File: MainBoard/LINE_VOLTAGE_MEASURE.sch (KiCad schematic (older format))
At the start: 19 parts

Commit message: R0.1
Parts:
- removed D?: D, symbol Device:D
- removed D?: 6V, symbol Device:D_Zener
- removed R?: 1k, symbol Device:R
- removed R?: 1M, symbol Device:R
- removed R?: 25k, symbol Device:R
- removed U? (x5): LMV324, symbol Amplifier_Operational:LMV324
- added C?: 0.1uF, symbol Device:C
- added D?: 1N750, symbol Device:D_Zener
- added D?: D_Schottky, symbol Device:D_Schottky
- added R?: 1M, symbol Device:R
- added R?: 68, symbol Device:R
- added U? (x4): MCP6004, symbol Amplifier_Operational:MCP6004
- C?: value 33uF -> 10uF
- R?: value 1M -> 560k
- R?: value 15k -> 12k
- R?: value 4.7k -> 15k
- R?: footprint (none) -> Option in Mechatronics
- R?: value 4.7k -> 500k
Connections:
- net labels added: +6V
- net labels removed: +12V
- wire segments 62 -> 59
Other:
- note added: "A"
- note added: "A (Vrms)\n2.098\n2.308\n2.517\n2.727\n2.937\n"
- note added: "B"
- note added: "B (VDC)\n2.967\n3.264\n3.560\n3.857\n4.154"
- note added: "C"
- note added: "C (VDC)\n0.367\n1.109\n1.851\n2.592\n3.334\n"
- note added: "LINE (Vrms)\n100\n110\n120\n130\n140\n"
- moved on the sheet: C?, R?

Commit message: Layout Main Board
Layout main PCB
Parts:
- removed R?: 4.7k, symbol Device:R
- removed R?: 1M, symbol Device:R
- removed R?: 500k, symbol Device:R
- added J7: CENTER TAP, Connector_PinHeader_2.54mm:PinHeader_1x01_P2.54mm_Vertical, symbol Connector:Screw_Terminal_01x01
- added J8: NEUTRAL, Connector_PinHeader_2.54mm:PinHeader_1x01_P2.54mm_Vertical, symbol Connector:Screw_Terminal_01x01
- added J9: LINE, Connector_PinHeader_2.54mm:PinHeader_1x01_P2.54mm_Vertical, symbol Connector:Screw_Terminal_01x01
- added R17, R18, R20: 1M, Resistor_THT:R_Axial_DIN0204_L3.6mm_D1.6mm_P7.62mm_Horizontal, symbol Device:R
- added R22: 10k, Resistor_THT:R_Axial_DIN0204_L3.6mm_D1.6mm_P7.62mm_Horizontal, symbol Device:R
- added R34, R35, R36, R37, R38, R39: 27k, Resistor_THT:R_Axial_DIN0204_L3.6mm_D1.6mm_P7.62mm_Horizontal, symbol Device:R
- added unit 4 of U4
- C10, C11, C12: renamed from C?; footprint (none) -> Capacitor_THT:CP_Radial_D5.0mm_P2.00mm; P/N (none) -> 732-8625-1-ND
- C9: renamed from C?; footprint (none) -> Capacitor_THT:C_Rect_L4.0mm_W2.5mm_P2.50mm
- D3: renamed from D?; value D_Schottky -> SB140TA; footprint (none) -> Diode_THT:D_DO-41_SOD81_P10.16mm_Horizontal; P/N (none) -> SB140TA
- D4: renamed from D?; footprint (none) -> Diode_THT:D_DO-35_SOD27_P10.16mm_Horizontal; P/N (none) -> 1514-1N750ABKPBFREE-ND
- R14: renamed from R?; footprint (none) -> Resistor_THT:R_Axial_DIN0207_L6.3mm_D2.5mm_P10.16mm_Horizontal
- R15: renamed from R?; value 12k -> 10k; footprint (none) -> Resistor_THT:R_Axial_DIN0204_L3.6mm_D1.6mm_P7.62mm_Horizontal
- R16, R21: renamed from R?; footprint (none) -> Resistor_THT:R_Axial_DIN0204_L3.6mm_D1.6mm_P7.62mm_Horizontal
- R19: renamed from R?; footprint Option in Mechatronics -> Resistor_THT:R_Axial_DIN0204_L3.6mm_D1.6mm_P7.62mm_Horizontal
- U4: renamed from U?; footprint (none) -> Package_DIP:DIP-14_W7.62mm_LongPads
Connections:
- net GND: now also R17.1, R35.1, R38.1
- net LINE_ADC: now also R22.1
- net LINE_PHASE: now also R34.1, R35.2; no longer U4.8
- net HV_CNTR_TAP: now reaches R14.2, R15.1
- net HV_CNTR_TAP: now also J7.1 (Pin_1), R36.2; no longer U4.10 (+), U4.3 (+)
- net CUR_PEAK_OUT: now reaches C10.1, D3.1 (K), U4.2 (-)
- net CUR_PEAK_OUT: now also U4.10 (+), R18.2, R20.2; no longer U4.5 (+)
- net at C11.1, R21.1: now also U4.8, R22.2; no longer U4.7
- net at R19.1, R21.2: now also U4.9 (-); no longer U4.6 (-)
- net VREF_4_7: now reaches D4.1 (K), R16.2, R19.2
- net LINE_IN+ renamed HV_IN
- net HV_IN: now also J9.1 (Pin_1)
- net LINE_IN- renamed HV_NEUTRAL
- net HV_NEUTRAL: now also J8.1 (Pin_1), R37.1
- new net: R39.1, U4.14, U4.3 (+), U4.5 (+)
- new net: R17.2, R18.1, R20.1, U4.6 (-)
- new net: R34.2, U4.7
- new net: R37.2, R38.2, U4.12 (+)
- new net: R36.1, R39.2, U4.13 (-)
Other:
- note added: "2 / 3 RATIO"
- note added: "LINE to ground: 100-140Vrms\n"
- note removed: "LINE_IN to ground: 100-130V\n"
- moved on the sheet: C10, C11, C12, C9, D3, D4, R14, R15, R16, R19, R21, U4A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

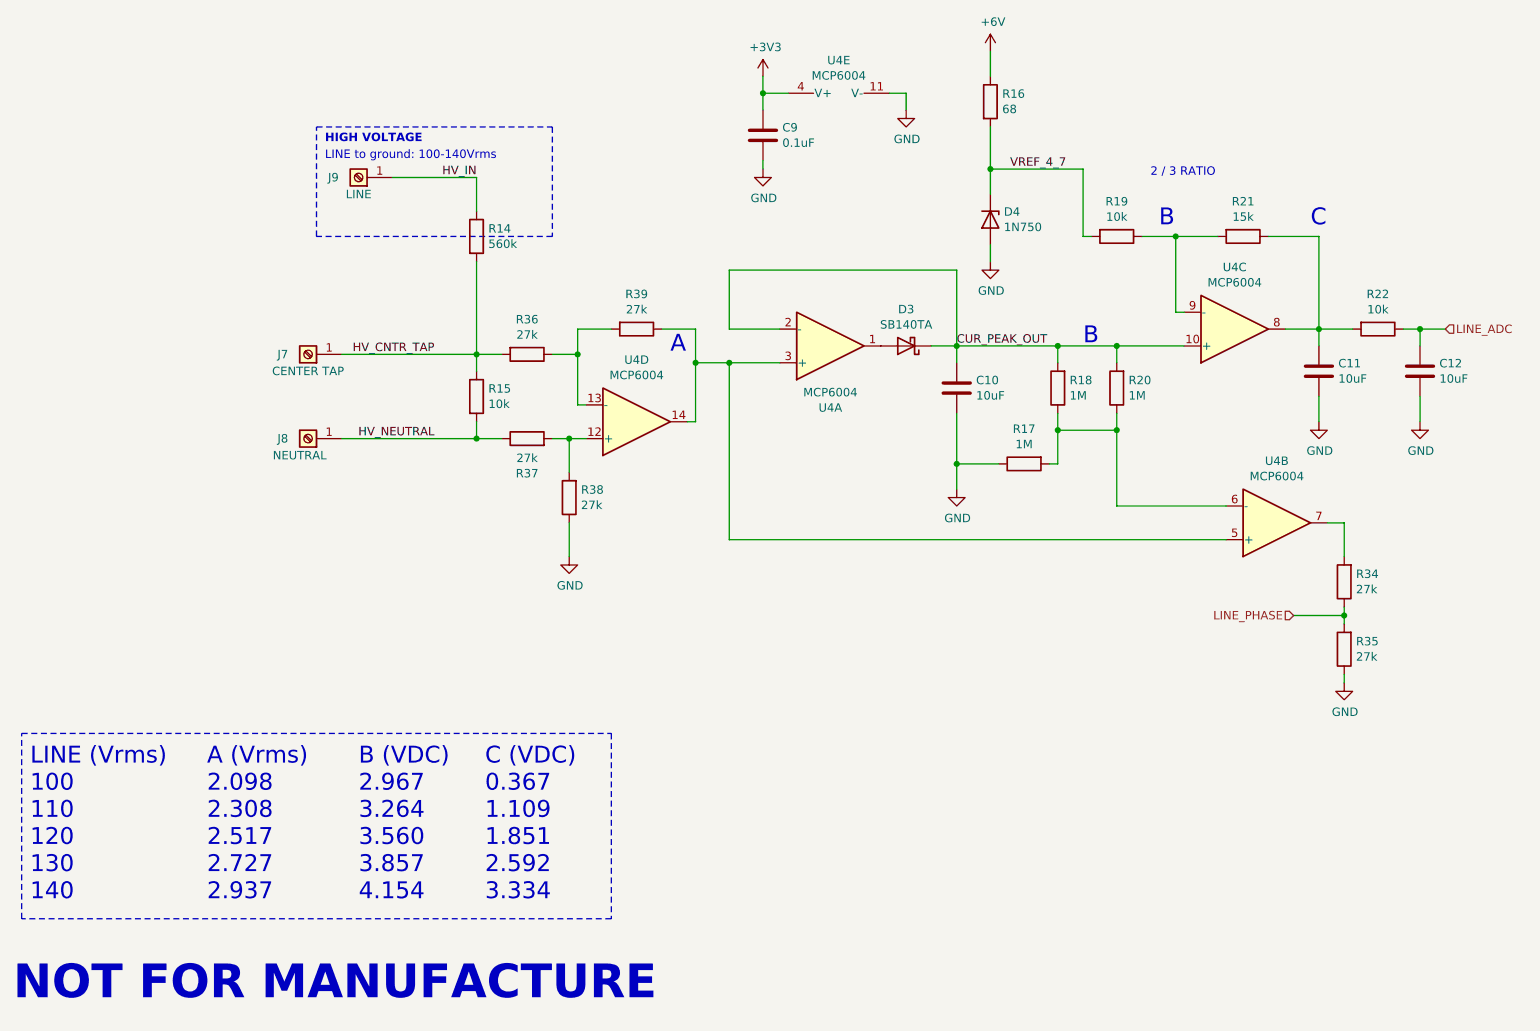
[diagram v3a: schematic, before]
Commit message: Update Voltage calculation
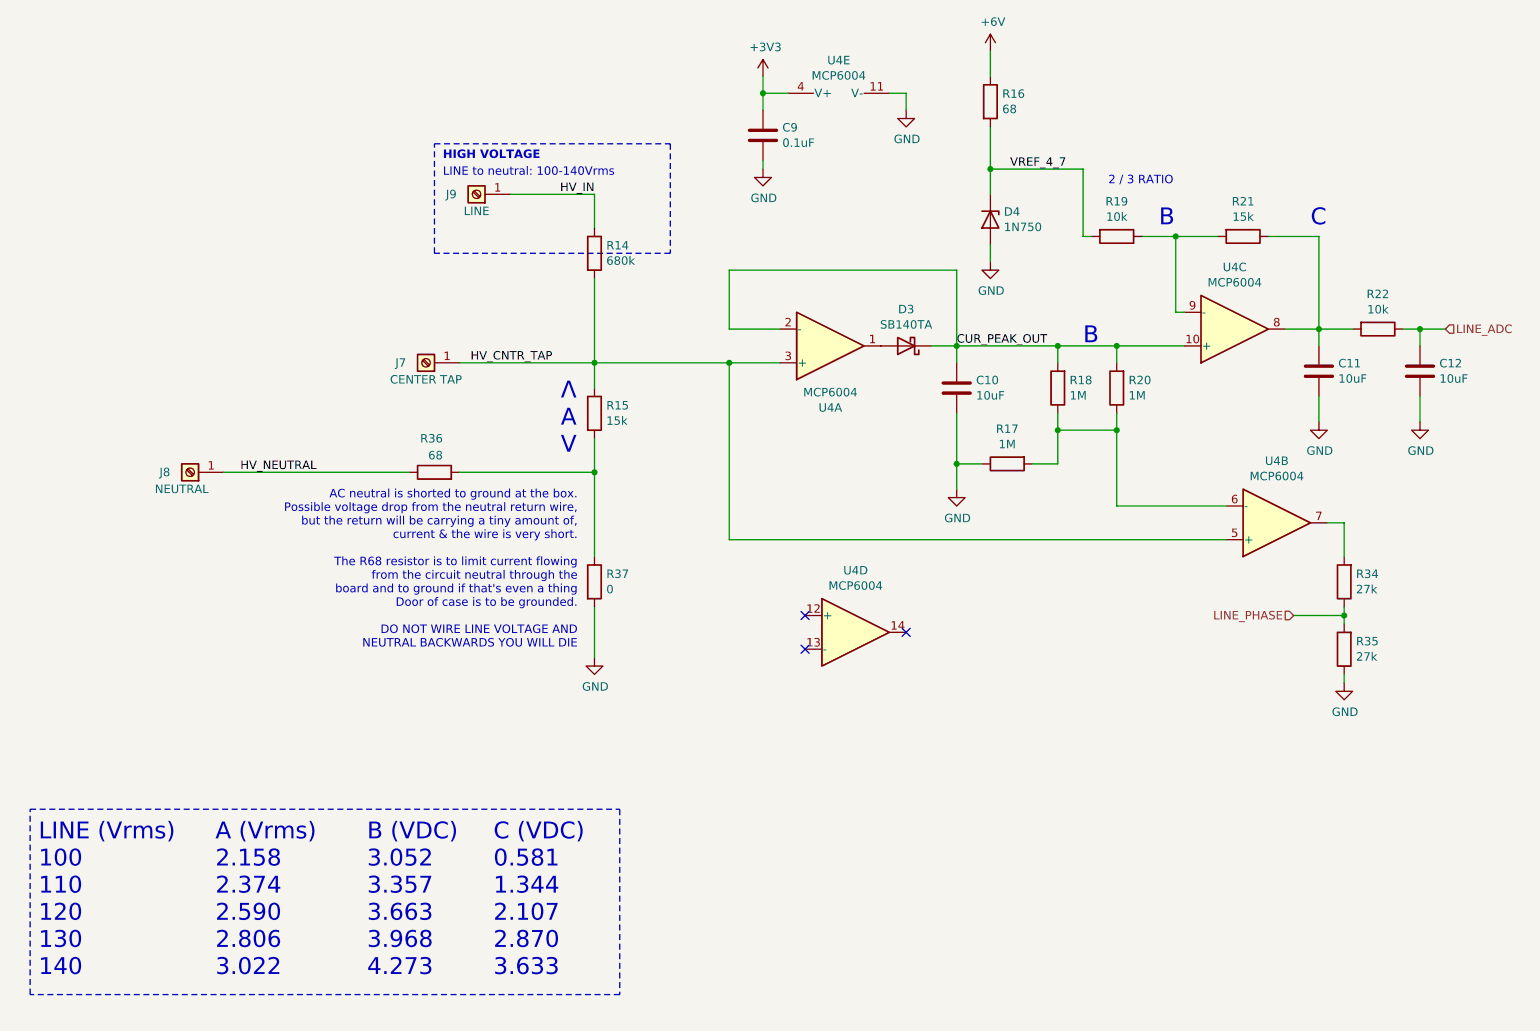
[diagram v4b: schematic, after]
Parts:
- removed R38, R39: 27k, Resistor_THT:R_Axial_DIN0204_L3.6mm_D1.6mm_P7.62mm_Horizontal, symbol Device:R
- R14: value 560k -> 680k
- R15: value 10k -> 15k
- R36: value 27k -> 68
- R37: value 27k -> 0
- U4: footprint Package_DIP:DIP-14_W7.62mm_LongPads -> (none)
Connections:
- net GND: now also R37.2
- net HV_CNTR_TAP: now also U4.3 (+), U4.5 (+); no longer R36.2
- net HV_NEUTRAL: now also R36.1; no longer R15.2, R37.1
- net at U4.12 (+): no longer R37.2
- net at U4.13 (-): no longer R36.1
- new net: R15.2, R36.2, R37.1
- now unconnected: U4.14
- no-connect marks 0 -> 3
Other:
- note added: "A (Vrms)\n2.158\n2.374\n2.590\n2.806\n3.022\n"
- note added: "AC neutral is shorted to ground at the box.\nPossible voltage drop from the neutral return wire,\nbut the return will be carrying a tiny amount of,\n current & the wire is very short.\n\nThe R68 resistor is to limit current flowing\nfrom the circuit neutral through the\nboard and to ground if that's even a thing\nDoor of case is to be grounded.\n\nDO NOT WIRE LINE VOLTAGE AND\n NEUTRAL BACKWARDS 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"
- note added: "B (VDC)\n3.052\n3.357\n3.663\n3.968\n4.273\n"
- note added: "C (VDC)\n0.581\n1.344\n2.107\n2.870\n3.633\n"
- note added: "LINE to neutral: 100-140Vrms\n"
- note added: "Ʌ\nA\nV"
- note removed: "A"
- note removed: "A (Vrms)\n2.098\n2.308\n2.517\n2.727\n2.937\n"
- note removed: "B (VDC)\n2.967\n3.264\n3.560\n3.857\n4.154"
- note removed: "C (VDC)\n0.367\n1.109\n1.851\n2.592\n3.334\n"
- note removed: "LINE to ground: 100-140Vrms\n"
- note removed: "NOT FOR MANUFACTURE"
- moved on the sheet: J7, J8, J9, R14, R15, R17
